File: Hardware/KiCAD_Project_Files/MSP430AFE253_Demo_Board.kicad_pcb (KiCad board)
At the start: 4 copper layers, 25.4 x 50.8 mm, 42 parts, among them J1 USB_MINI_B, P1 POWER, P2 3.3V, P3 HEADER_1X4, P4 TX, P5 RX, P6 DEBUG, SW1 FSMSM, SW2 FSMSM, U1 FT230XQ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

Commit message: First commit at Rev 4
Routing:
- added copper zone on B.Cu, net (none)
- added copper zone on F.Cu, net (none)
- removed copper zone on B.Cu, net NoConnection1
- removed copper zone on F.Cu, net NoConnection1
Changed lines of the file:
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@@
     (area 145.046095 70.8152 178.768 127.190501)
     (thickness 1.6002)
-    (drawings 46)
+    (drawings 48)
     (tracks 374)
     (zones 0)
@@
   )
   (layers
-    (15 Front signal)
+    (15 Front signal hide)
     (2 3V3.Cu power hide)
     (1 GND.Cu power hide)
-    (0 Back signal)
+    (0 Back signal hide)
     (16 B.Adhes user)
     (17 F.Adhes user)
     (18 B.Paste user)
     (19 F.Paste user)
-    (20 B.SilkS user)
+    (20 B.SilkS user hide)
     (21 F.SilkS user)
     (22 B.Mask user)
@@
       (outputdirectory P:/Engineering_SECURE/Projects/MSP430AFE253_Demo_Board/Hardware/Gerbers/Rev3/))
   )
-  (net 0 NoConnection1)
+  (net 0 "")
   (net 1 +5V)
   (net 2 /A0N)
@@
     (uvia_dia 0.508)
     (uvia_drill 0.127)
+    (add_net "")
     (add_net /A0N)
     (add_net /A0P)
@@
     (add_net N-000008)
     (add_net N-000009)
-    (add_net NoConnection1)
     (add_net XT2IN)
     (add_net XT2OUT)
@@
     )
   )
+  (gr_text RX (at 169.545 83.312 90) (layer F.SilkS)
+    (effects (font (size 1.016 1.016) (thickness 0.2032)))
+  )
+  (gr_text TX (at 166.37 83.312 90) (layer F.SilkS)
+    (effects (font (size 1.016 1.016) (thickness 0.2032)))
+  )
   (gr_text GND (at 156.21 120.65 90) (layer B.SilkS)

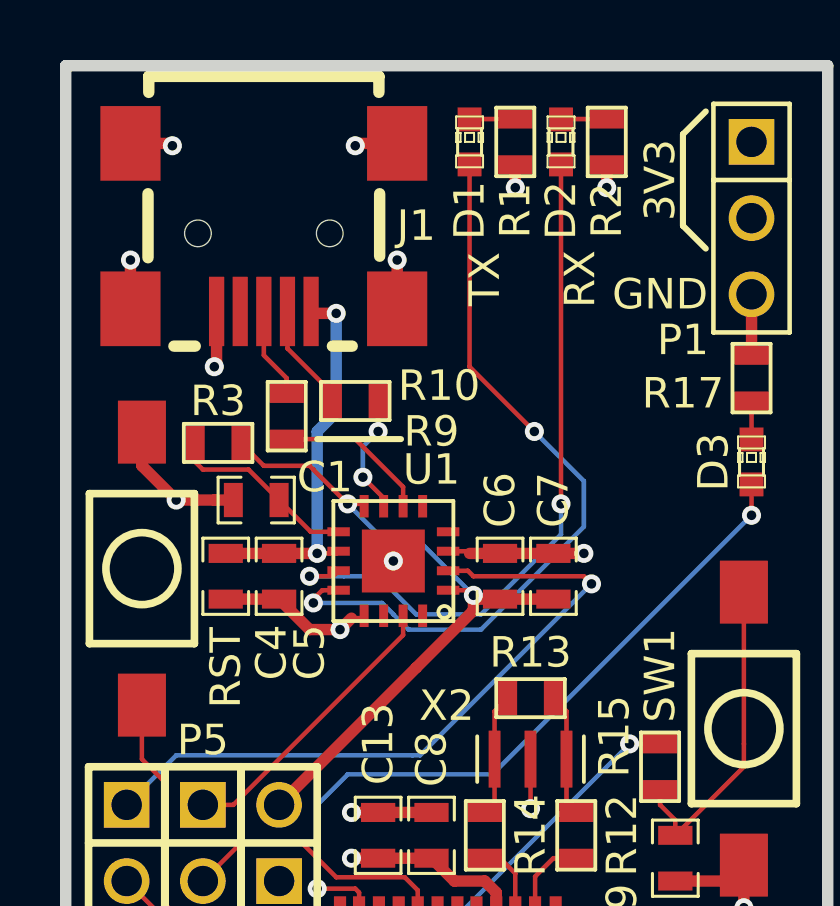
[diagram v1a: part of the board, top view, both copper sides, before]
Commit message: Updated Schematic and Board design for corrected TX LED connection
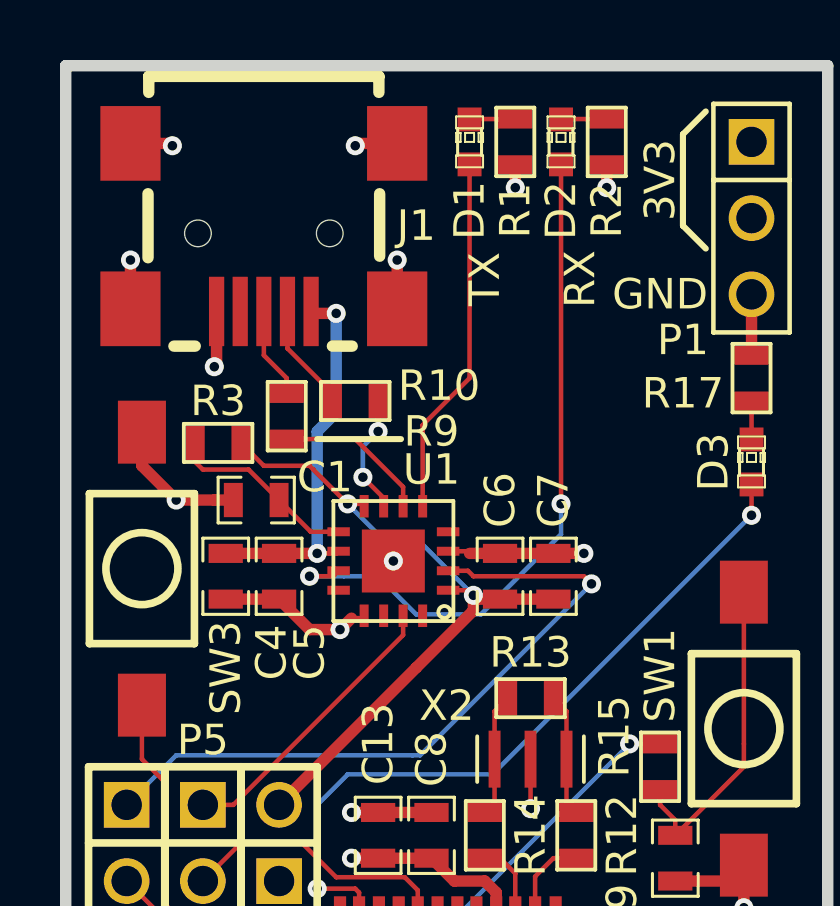
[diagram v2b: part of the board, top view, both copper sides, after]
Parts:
- C1, C10, C2, C5, C6, C9: value .1u -> 0.1u
- X2: value 8MHz -> 3.68MHz
- renumbered RST to SW3
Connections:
- D1 pad 1: N-0000015 (its old number) -> N-0000026
- U1 pad 12: N-0000015 (its old number) -> (no net)
- U1 pad 5: (no net) -> N-0000026
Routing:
- net N-0000015 (its old number): track 25.6 -> 0.00 mm, vias 2 -> 0
- net N-0000026: track 0.00 -> 12.0 mm

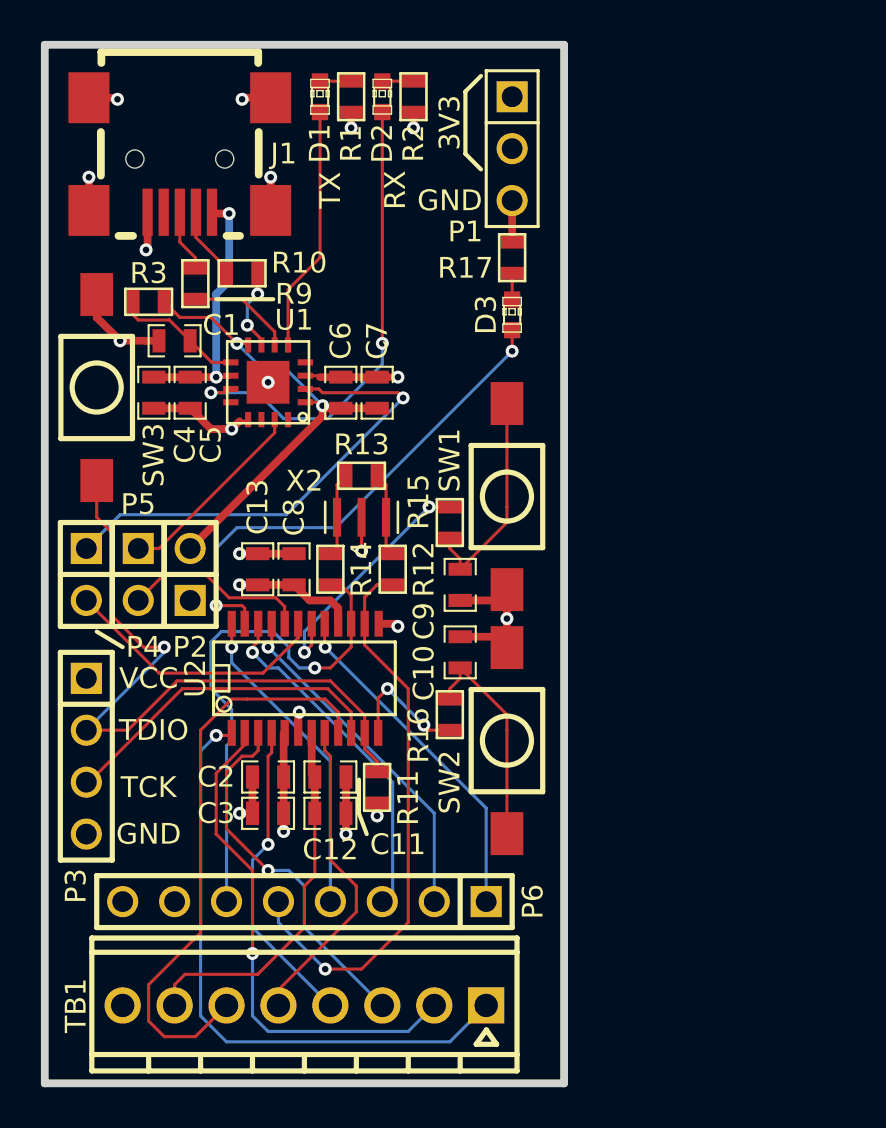
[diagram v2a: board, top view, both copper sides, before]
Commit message: Check in current state of Rev 4 design (in-progress) before checking out and forking the Rev 1 design.
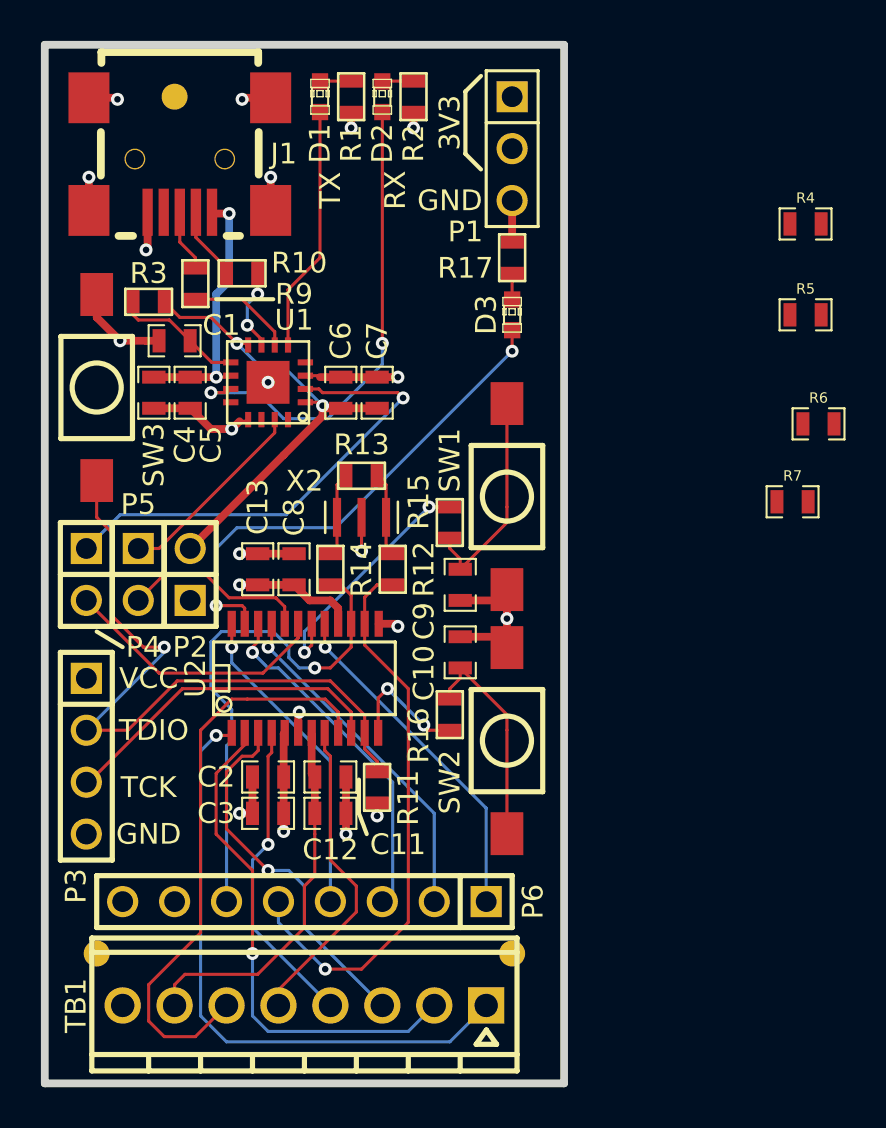
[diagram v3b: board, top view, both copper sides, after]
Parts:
- added ?: , FIDUCIAL, F.Cu at (158.8, 78.7)
- added ?: , FIDUCIAL, F.Cu at (175.3, 120.7)
- added ?: , FIDUCIAL, F.Cu at (154.9, 120.7)
- added R4: 1k, 0603, F.Cu at (189.6, 85.0)
- added R5: 1k, 0603, F.Cu at (189.6, 89.4)
- added R6: 1k, 0603, F.Cu at (190.2, 94.7)
- added R7: 1k, 0603, F.Cu at (189.0, 98.6)
- R1, R2: value 1.8k -> 270
- R15, R16: value 47k -> 1
- X2: value 3.68MHz -> 8MHz
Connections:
- C10 pad 1: N-000005 (its old number) -> N-0000021
- C9 pad 1: N-0000024 (its old number) -> N-0000022
- P4 pad 1: N-000001 (its old number) -> N-0000014
- P4 pad 2: N-0000035 -> N-0000018
- P5 pad 2: N-000008 (its old number) -> N-0000016
- R15 pad 1: N-000006 -> N-0000022
- R15 pad 2: N-0000024 (its old number) -> N-0000013
- R16 pad 1: N-000007 (its old number) -> N-0000021
- R16 pad 2: N-000005 (its old number) -> N-0000020
- SW1 pad 1: N-0000024 (its old number) -> N-0000013
- SW2 pad 1: N-000005 (its old number) -> N-0000020
- U1 pad 15: N-0000011 -> N-0000015
- U1 pad 2: N-000001 (its old number) -> N-0000033
- U2 pad 12: N-000007 (its old number) -> N-0000020
- U2 pad 18: N-000006 -> N-0000013
- U2 pad 19: N-0000035 -> N-0000019
- U2 pad 20: N-000008 (its old number) -> N-0000017
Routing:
- net N-000001 (its old number): track 23.5 -> 0.00 mm, vias 1 -> 0
- net N-0000014: track 0.00 -> 18.5 mm, vias 0 -> 1
- net N-0000013: track 0.00 -> 18.2 mm, vias 0 -> 2
- net N-0000035: track 13.2 -> 0.00 mm
- net N-0000018: track 0.00 -> 12.6 mm
- net N-0000020: track 0.00 -> 12.3 mm, vias 0 -> 2
- net N-000006: track 12.2 -> 0.00 mm, vias 2 -> 0
- net N-0000024 (its old number): track 10.8 -> 0.00 mm
- net N-000005 (its old number): track 10.8 -> 0.00 mm
- net N-000008 (its old number): track 9.18 -> 0.00 mm
- net N-0000016: track 0.00 -> 8.34 mm
- net N-000007 (its old number): track 6.42 -> 0.00 mm, vias 2 -> 0
- net N-0000033: track 0.00 -> 4.96 mm
- net N-0000021: track 0.00 -> 4.94 mm
- net N-0000022: track 0.00 -> 4.76 mm
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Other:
- board text added: "Changes: Added fiducials Added resistors on either side of Rx/Tx jumpers Added 3 jumpers to BOM Corrected resonator on BOM Changed NPTH's in USB connector to PTH's Fixed connection to D1 on USB-to-Serial adapter"
- board text added: "To do: Bring unused FTDI IO out to pad."

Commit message: Final commit for Rev4 release
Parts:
- removed ? (x3): , FIDUCIAL
- removed C10, C9: 0.1u, 0603
- removed R15, R16: 1, SM0603
- removed R4, R5, R6, R7: 1k, 0603
- added TP1: 5015, TP_PAD_SMT_5015, B.Cu at (170.2, 87.4)
- added TP2: 5015, TP_PAD_SMT_5015, B.Cu at (167.6, 87.4)
- added TP3: 5015, TP_PAD_SMT_5015, B.Cu at (175.3, 87.4)
- added TP4: 5015, TP_PAD_SMT_5015, B.Cu at (172.7, 87.4)
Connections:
- P4 pad 1: N-0000014 (its old number) -> N-0000015
- P4 pad 2: N-0000018 -> N-000005
- P5 pad 1: N-0000011 (its old number) -> N-000004
- P5 pad 2: N-0000016 -> N-000006
- U1 pad 12: (no net) -> N-0000025
- U1 pad 14: (no net) -> N-0000024
- U1 pad 15: N-0000015 -> N-000004
- U1 pad 16: (no net) -> N-0000027
- U1 pad 2: N-0000033 -> N-0000015
- U1 pad 4: (no net) -> N-0000026
- U2 pad 19: N-0000019 (its old number) -> N-000005
- U2 pad 20: N-0000017 (its old number) -> N-000006
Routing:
- net N-0000015: track 0.64 -> 25.0 mm, vias 0 -> 1
- net N-0000025: track 0.00 -> 23.0 mm, vias 0 -> 1
- net N-0000024: track 0.00 -> 19.5 mm, vias 0 -> 1
- net N-0000014 (its old number): track 18.5 -> 0.00 mm, vias 1 -> 0
- net N-000005: track 0.00 -> 13.2 mm
- net N-0000018: track 12.6 -> 0.00 mm
- net N-0000027: track 0.00 -> 12.4 mm, vias 0 -> 1
- net N-000004: track 0.00 -> 9.66 mm
- net N-000006: track 0.00 -> 9.18 mm
- net N-0000011 (its old number): track 9.02 -> 0.00 mm
- net N-0000016: track 8.34 -> 0.00 mm
- net N-0000026: track 0.00 -> 5.64 mm, vias 0 -> 1
- net N-0000033: track 4.96 -> 0.00 mm
- net N-0000021 (its old number): track 4.94 -> 0.00 mm
- net GND: track 46.0 -> 41.2 mm
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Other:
- board text added: "Changes: Added fiducials Added resistors on either side of Rx/Tx jumpers Added 3 jumpers to BOM Corrected resonator on BOM Changed NPTH's in USB connector to PTH's Fixed connection to D1 on USB-to-Serial adapter Added pads for breaking out extra unused FTDI pins"
- board text removed: "Changes: Added fiducials Added resistors on either side of Rx/Tx jumpers Added 3 jumpers to BOM Corrected resonator on BOM Changed NPTH's in USB connector to PTH's Fixed connection to D1 on USB-to-Serial adapter"
- board text removed: "To do: Bring unused FTDI IO out to pad."

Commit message: Forgot to update rev info on back silkscreen
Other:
- board text added: "MSP430AFE253 DEV CASCOLOGIX.COM REV4"
- board text removed: "MSP430AFE253 DEV CASCOLOGIX.COM REV3"
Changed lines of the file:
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@@
   (page USLetter)
   (title_block
+    (title "MSP430AFE253 Development Board")
     (date "Saturday, August 23, 2014")
+    (rev 4)
+    (company "Casco Logix")
   )
   (layers
-    (15 Front signal)
-    (2 3V3.Cu power)
-    (1 GND.Cu power)
+    (15 Front signal hide)
+    (2 3V3.Cu power hide)
+    (1 GND.Cu power hide)
     (0 Back signal)
     (16 B.Adhes user)
@@
     (19 F.Paste user)
     (20 B.SilkS user)
-    (21 F.SilkS user)
+    (21 F.SilkS user hide)
     (22 B.Mask user)
     (23 F.Mask user)
@@
   (gr_line (start 163.576 88.646) (end 160.782 88.646) (angle 90) (layer F.SilkS) (width 0.2032))
   (gr_line (start 156.21 105.664) (end 154.94 104.902) (angle 90) (layer F.SilkS) (width 0.2032))
-  (gr_text "MSP430AFE253 DEV\nCASCOLOGIX.COM\nREV3" (at 163.83 100.076 90) (layer B.SilkS)
+  (gr_text "MSP430AFE253 DEV\nCASCOLOGIX.COM\nREV4" (at 163.83 100.076 90) (layer B.SilkS)
     (effects (font (thickness 0.254)) (justify mirror))
   )

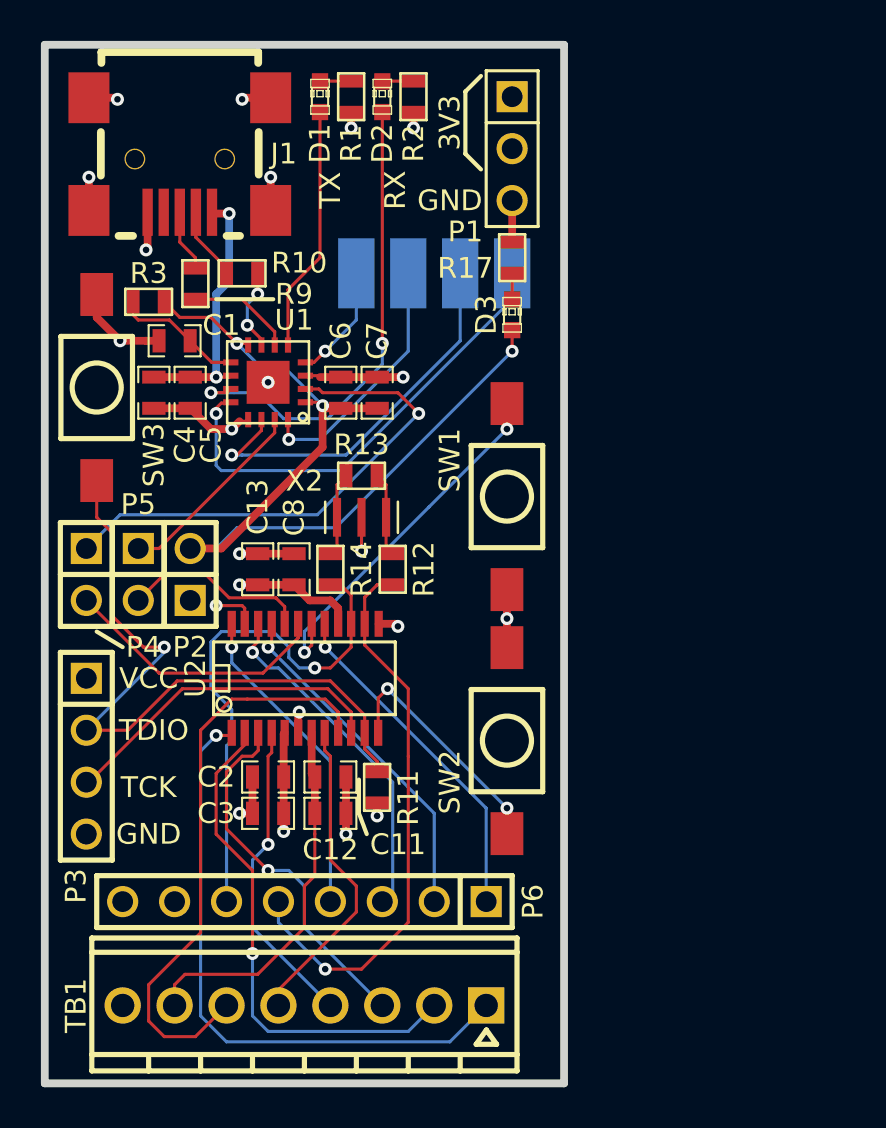
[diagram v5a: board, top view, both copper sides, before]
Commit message: Rev 5 Commit. Generated new board gerbers and drawings. Updated user guide documentation and board renderings.
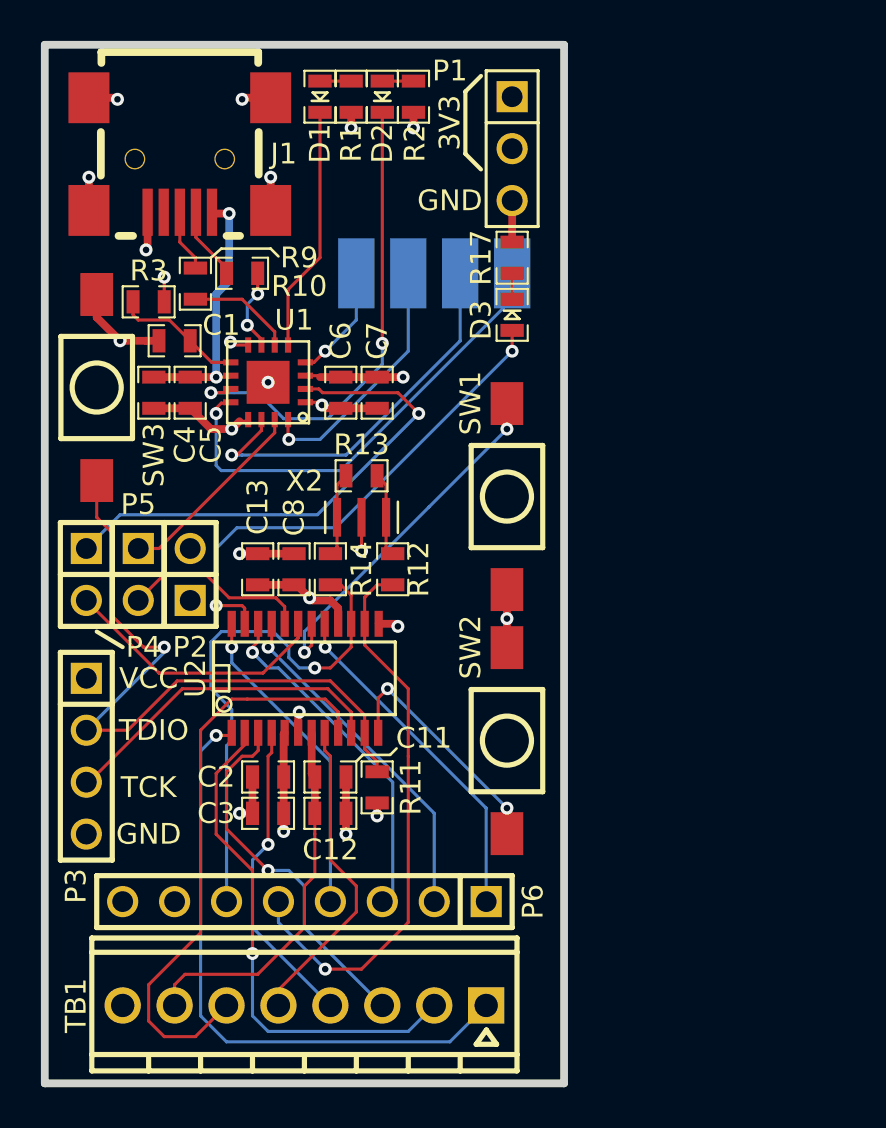
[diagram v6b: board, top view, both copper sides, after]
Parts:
- D1: value GREEN -> GRN; footprint LED-0603 -> D0603
- D2, D3: footprint LED-0603 -> D0603
- R1, R10, R11, R12, R13, R14, R17, R2, R3, R9: footprint SM0603 -> 0603
- turned D3 to 270 degrees
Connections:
- C6 pad 1: N-0000019 (its old number) -> VCCIO
- C7 pad 1: N-0000019 (its old number) -> VCCIO
- P2 pad 2: N-0000019 (its old number) -> VCCIO
- R1 pad 1: GND -> VCCIO
- R1 pad 2: N-0000036 -> N-0000027
- R17 pad 1: N-0000012 (its old number) -> N-0000028
- R2 pad 1: GND -> VCCIO
- R2 pad 2: N-0000010 (its old number) -> N-0000026
- R3 pad 1: N-0000019 (its old number) -> VCCIO
- U1 pad 1: N-0000019 (its old number) -> VCCIO
- U1 pad 11: N-0000020 -> N-0000017
- U1 pad 5: N-0000013 (its old number) -> N-0000024
- U1 pad 8: N-0000019 (its old number) -> VCCIO
- U2 pad 23: N-000007 -> N-0000036
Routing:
- net N-0000019 (its old number): track 24.9 -> 0.00 mm, vias 2 -> 0
- net N-000007: track 24.5 -> 0.00 mm, vias 2 -> 0
- net N-0000020: track 23.4 -> 0.00 mm, vias 2 -> 0
- net N-0000017: track 0.00 -> 23.4 mm, vias 0 -> 2
- net N-0000036: track 1.53 -> 24.5 mm, vias 0 -> 2
- net N-0000024: track 0.00 -> 12.0 mm
- net N-0000013 (its old number): track 12.0 -> 0.00 mm
- net VCCIO: track 0.00 -> 7.64 mm, vias 0 -> 5
- net N-0000027: track 0.00 -> 1.53 mm
- net N-0000026: track 0.00 -> 1.53 mm
- net N-0000010 (its old number): track 1.53 -> 0.00 mm
- net GND: track 41.2 -> 39.7 mm, vias 18 -> 16
- net N-0000028: track 0.00 -> 1.28 mm
- net N-0000012 (its old number): track 1.28 -> 0.00 mm
- net VCC: track 11.5 -> 10.7 mm
- added copper zone on 3V3.Cu, net VCCIO
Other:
- rule pad_to_mask_clearance: 0.254 -> 0.0508
- board text added: "MSP430AFE253 DEV CASCOLOGIX.COM REV5"
- board text removed: "Changes: Added fiducials Added resistors on either side of Rx/Tx jumpers Added 3 jumpers to BOM Corrected resonator on BOM Changed NPTH's in USB connector to PTH's Fixed connection to D1 on USB-to-Serial adapter Added pads for breaking out extra unused FTDI pins"
- board text removed: "MSP430AFE253 DEV CASCOLOGIX.COM REV4"
